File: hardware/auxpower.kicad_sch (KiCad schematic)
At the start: 6 parts

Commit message: review ts
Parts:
- renumbered D22 to D2, D23 to D3, R94 to R13, R95 to R14, TP21 to TP2, TP22 to TP3
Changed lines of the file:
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@@
 		(dnp no)
 		(fields_autoplaced yes)
-		(property "Reference" "R94"
+		(property "Reference" "R13"
 			(at 22.86 118.1099 0)
 			(show_name no)
@@
 			(project "PS-LVCarrier"
 				(path "/9bab2d9d-20f3-40ef-8545-e1299efec47e/194a8848-c0d2-44dd-9e5b-1946509490d6"
-					(reference "R94")
+					(reference "R13")
 					(unit 1)
 				)
@@
 		(dnp no)
 		(fields_autoplaced yes)
-		(property "Reference" "D23"
+		(property "Reference" "D3"
 			(at 39.37 124.3964 90)
 			(show_name no)
@@
 			(project "PS-LVCarrier"
 				(path "/9bab2d9d-20f3-40ef-8545-e1299efec47e/194a8848-c0d2-44dd-9e5b-1946509490d6"
-					(reference "D23")
+					(reference "D3")
 					(unit 1)
 				)
@@
 		(dnp no)
 		(fields_autoplaced yes)
-		(property "Reference" "D22"
+		(property "Reference" "D2"
 			(at 22.86 124.3964 90)
 			(show_name no)
@@
 			(project "PS-LVCarrier"
 				(path "/9bab2d9d-20f3-40ef-8545-e1299efec47e/194a8848-c0d2-44dd-9e5b-1946509490d6"
-					(reference "D22")
+					(reference "D2")
 					(unit 1)
 				)
@@
 		(dnp no)
 		(fields_autoplaced yes)
-		(property "Reference" "#PWR087"
+		(property "Reference" "#PWR018"
 			(at 20.32 119.38 0)
 			(hide yes)
@@
 			(project "PS-LVCarrier"
 				(path "/9bab2d9d-20f3-40ef-8545-e1299efec47e/194a8848-c0d2-44dd-9e5b-1946509490d6"
-					(reference "#PWR087")
+					(reference "#PWR018")
 					(unit 1)
 				)
@@
 		(in_pos_files yes)
 		(dnp no)
-		(property "Reference" "#PWR092"
+		(property "Reference" "#PWR023"
 			(at 157.48 64.77 0)
 			(hide yes)
@@
 			(project "PS-LVCarrier"
 				(path "/9bab2d9d-20f3-40ef-8545-e1299efec47e/194a8848-c0d2-44dd-9e5b-1946509490d6"
-					(reference "#PWR092")
+					(reference "#PWR023")
 					(unit 1)
 				)
@@
 		(dnp no)
 		(fields_autoplaced yes)
-		(property "Reference" "R95"
+		(property "Reference" "R14"
 			(at 39.37 118.1099 0)
 			(show_name no)
@@
 			(project "PS-LVCarrier"
 				(path "/9bab2d9d-20f3-40ef-8545-e1299efec47e/194a8848-c0d2-44dd-9e5b-1946509490d6"
-					(reference "R95")
+					(reference "R14")
 					(unit 1)
 				)
@@
 		(in_pos_files yes)
 		(dnp no)
-		(property "Reference" "#PWR088"
+		(property "Reference" "#PWR019"
 			(at 36.83 119.38 0)
 			(hide yes)
@@
 			(project "PS-LVCarrier"
 				(path "/9bab2d9d-20f3-40ef-8545-e1299efec47e/194a8848-c0d2-44dd-9e5b-1946509490d6"
-					(reference "#PWR088")
+					(reference "#PWR019")
 					(unit 1)
 				)
@@
 		(dnp no)
 		(fields_autoplaced yes)
-		(property "Reference" "#PWR089"
+		(property "Reference" "#PWR020"
 			(at 63.5 123.19 0)
 			(hide yes)
@@
 			(project "PS-LVCarrier"
 				(path "/9bab2d9d-20f3-40ef-8545-e1299efec47e/194a8848-c0d2-44dd-9e5b-1946509490d6"
-					(reference "#PWR089")
+					(reference "#PWR020")
 					(unit 1)
 				)
@@
 		(in_pos_files yes)
 		(dnp no)
-		(property "Reference" "#PWR090"
+		(property "Reference" "#PWR021"
 			(at 74.93 123.19 0)
 			(hide yes)
@@
 			(project "PS-LVCarrier"
 				(path "/9bab2d9d-20f3-40ef-8545-e1299efec47e/194a8848-c0d2-44dd-9e5b-1946509490d6"
-					(reference "#PWR090")
+					(reference "#PWR021")
 					(unit 1)
 				)
@@
 		(dnp no)
 		(fields_autoplaced yes)
-		(property "Reference" "TP22"
+		(property "Reference" "TP3"
 			(at 77.47 121.4119 0)
 			(show_name no)
@@
 			(project "PS-LVCarrier"
 				(path "/9bab2d9d-20f3-40ef-8545-e1299efec47e/194a8848-c0d2-44dd-9e5b-1946509490d6"
-					(reference "TP22")
+					(reference "TP3")
 					(unit 1)
 				)
@@
 		(dnp no)
 		(fields_autoplaced yes)
-		(property "Reference" "#PWR091"
+		(property "Reference" "#PWR022"
 			(at 110.49 64.77 0)
 			(hide yes)
@@
 			(project "PS-LVCarrier"
 				(path "/9bab2d9d-20f3-40ef-8545-e1299efec47e/194a8848-c0d2-44dd-9e5b-1946509490d6"
-					(reference "#PWR091")
+					(reference "#PWR022")
 					(unit 1)
 				)
@@
 		(dnp no)
 		(fields_autoplaced yes)
-		(property "Reference" "TP21"
+		(property "Reference" "TP2"
 			(at 66.04 121.4119 0)
 			(show_name no)
@@
 			(project "PS-LVCarrier"
 				(path "/9bab2d9d-20f3-40ef-8545-e1299efec47e/194a8848-c0d2-44dd-9e5b-1946509490d6"
-					(reference "TP21")
-					(unit 1)
-				)
+					(reference "TP2")
+					(unit 1)
+				)

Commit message: addressed
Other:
- sheet 12V -> 5V Buck Converter ports: added V_in_12V; removed V_in_24V
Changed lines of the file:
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@@
-			)
-		)
-		(pin "V_in_24V" input
-			(at 69.85 60.96 180)
-			(effects
-				(font
-					(size 1.27 1.27)
-				)
-				(justify left)
 			)
 		)
@@
 			)
 		)
+		(pin "V_in_12V" input
+			(at 69.85 60.96 180)
+			(effects
+				(font
+					(size 1.27 1.27)
+				)
+				(justify left)
+			)
+		)

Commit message: try smth on laptop
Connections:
- net +5V renamed 12V -> 5V Buck Converter/V_out_5V
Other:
- note removed: "Indicator LEDs"
- note removed: "Test Points"
- moved on the sheet: D2, D3, R13, R14, TP2, TP3

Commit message: craigenyah
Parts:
- renumbered D2 to D33, D3 to D34, R13 to R116, R14 to R117, TP2 to TP43, TP3 to TP44
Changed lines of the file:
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@@
 		(dnp no)
 		(fields_autoplaced yes)
-		(property "Reference" "R13"
+		(property "Reference" "R116"
 			(at 101.6 66.0399 0)
 			(show_name no)
@@
 			(project "PS-LVCarrier"
 				(path "/9bab2d9d-20f3-40ef-8545-e1299efec47e/194a8848-c0d2-44dd-9e5b-1946509490d6"
-					(reference "R13")
+					(reference "R116")
 					(unit 1)
 				)
@@
 		(dnp no)
 		(fields_autoplaced yes)
-		(property "Reference" "D3"
+		(property "Reference" "D34"
 			(at 156.21 72.3264 90)
 			(show_name no)
@@
 			(project "PS-LVCarrier"
 				(path "/9bab2d9d-20f3-40ef-8545-e1299efec47e/194a8848-c0d2-44dd-9e5b-1946509490d6"
-					(reference "D3")
+					(reference "D34")
 					(unit 1)
 				)
@@
 		(dnp no)
 		(fields_autoplaced yes)
-		(property "Reference" "D2"
+		(property "Reference" "D33"
 			(at 101.6 72.3264 90)
 			(show_name no)
@@
 			(project "PS-LVCarrier"
 				(path "/9bab2d9d-20f3-40ef-8545-e1299efec47e/194a8848-c0d2-44dd-9e5b-1946509490d6"
-					(reference "D2")
+					(reference "D33")
 					(unit 1)
 				)
@@
 		(in_pos_files yes)
 		(dnp no)
-		(property "Reference" "#PWR023"
+		(property "Reference" "#PWR045"
 			(at 147.32 64.77 0)
 			(hide yes)
@@
 			(project "PS-LVCarrier"
 				(path "/9bab2d9d-20f3-40ef-8545-e1299efec47e/194a8848-c0d2-44dd-9e5b-1946509490d6"
-					(reference "#PWR023")
+					(reference "#PWR045")
 					(unit 1)
 				)
@@
 		(dnp no)
 		(fields_autoplaced yes)
-		(property "Reference" "R14"
+		(property "Reference" "R117"
 			(at 156.21 66.0399 0)
 			(show_name no)
@@
 			(project "PS-LVCarrier"
 				(path "/9bab2d9d-20f3-40ef-8545-e1299efec47e/194a8848-c0d2-44dd-9e5b-1946509490d6"
-					(reference "R14")
+					(reference "R117")
 					(unit 1)
 				)
@@
 		(dnp no)
 		(fields_autoplaced yes)
-		(property "Reference" "TP3"
+		(property "Reference" "TP44"
 			(at 156.21 56.3879 0)
 			(show_name no)
@@
 			(project "PS-LVCarrier"
 				(path "/9bab2d9d-20f3-40ef-8545-e1299efec47e/194a8848-c0d2-44dd-9e5b-1946509490d6"
-					(reference "TP3")
+					(reference "TP44")
 					(unit 1)
 				)
@@
 		(dnp no)
 		(fields_autoplaced yes)
-		(property "Reference" "TP2"
+		(property "Reference" "TP43"
 			(at 101.6 56.3879 0)
 			(show_name no)
@@
 			(project "PS-LVCarrier"
 				(path "/9bab2d9d-20f3-40ef-8545-e1299efec47e/194a8848-c0d2-44dd-9e5b-1946509490d6"
-					(reference "TP2")
+					(reference "TP43")
 					(unit 1)
 				)

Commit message: switch, stll working
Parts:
- TP43, TP44: footprint TestPoint:TestPoint_THTPad_D3.0mm_Drill1.5mm -> TestPoint:TestPoint_Loop_D2.50mm_Drill1.0mm_LowProfile
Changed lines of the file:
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@@
 			)
 		)
-		(property "Footprint" "TestPoint:TestPoint_THTPad_D3.0mm_Drill1.5mm"
+		(property "Footprint" "TestPoint:TestPoint_Loop_D2.50mm_Drill1.0mm_LowProfile"
 			(at 158.75 60.96 0)
 			(hide yes)
@@
 			)
 		)
-		(property "Footprint" "TestPoint:TestPoint_THTPad_D3.0mm_Drill1.5mm"
+		(property "Footprint" "TestPoint:TestPoint_Loop_D2.50mm_Drill1.0mm_LowProfile"
 			(at 104.14 60.96 0)
 			(hide yes)

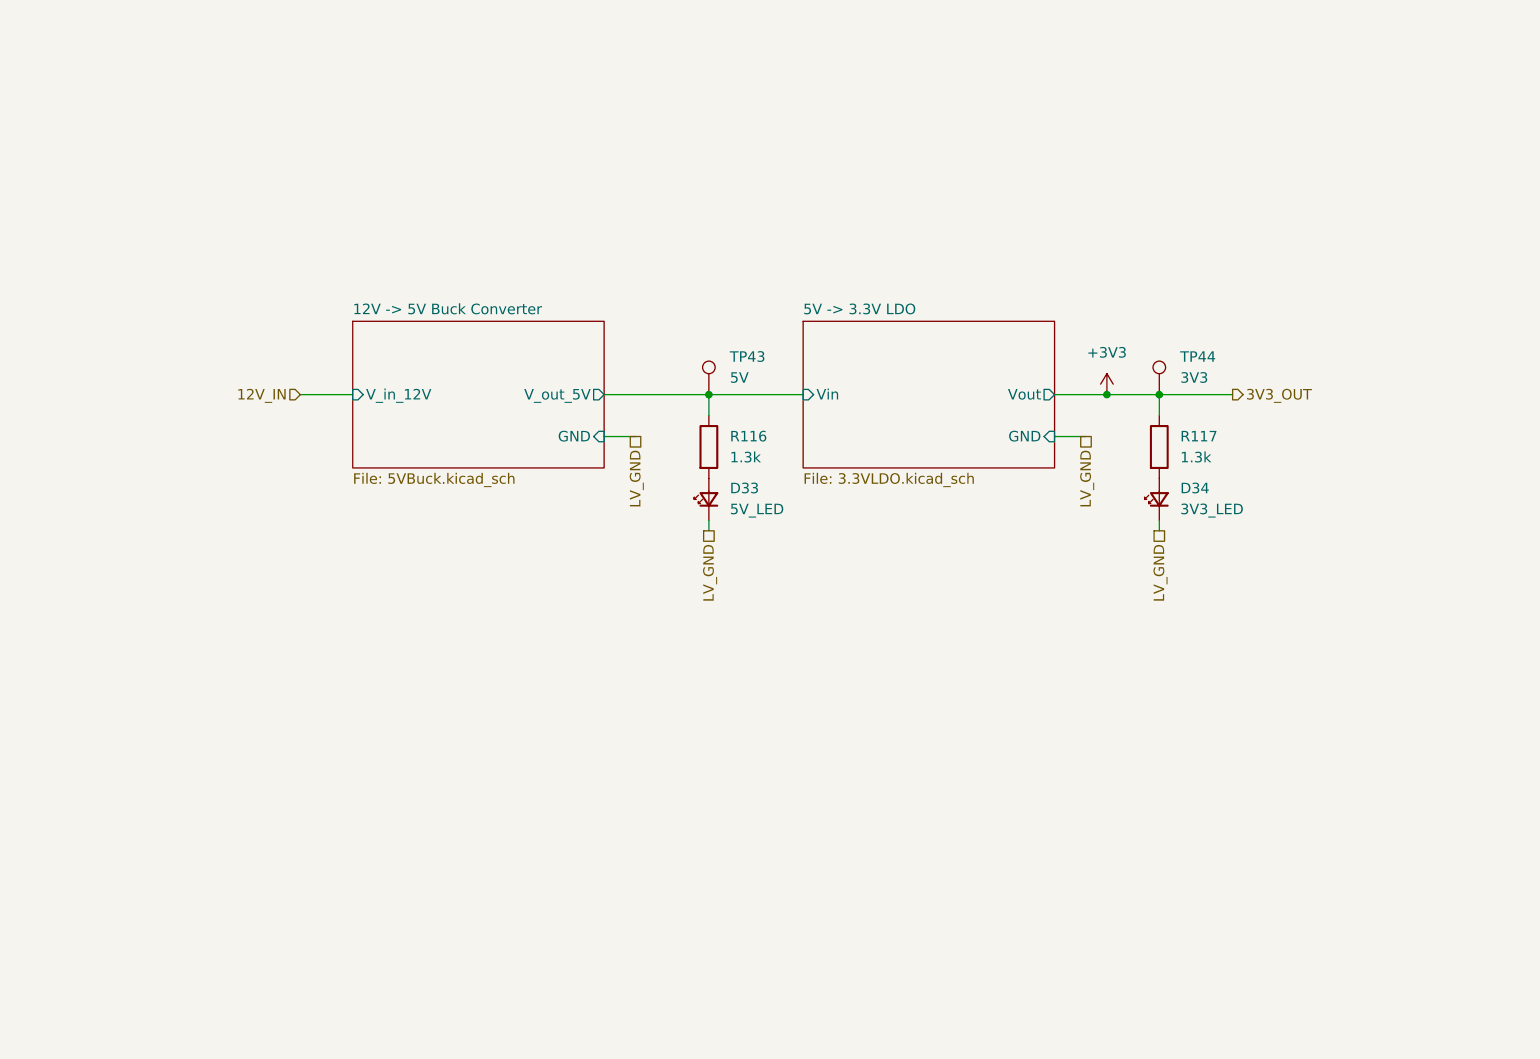
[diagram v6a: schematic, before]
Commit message: switch to laptop
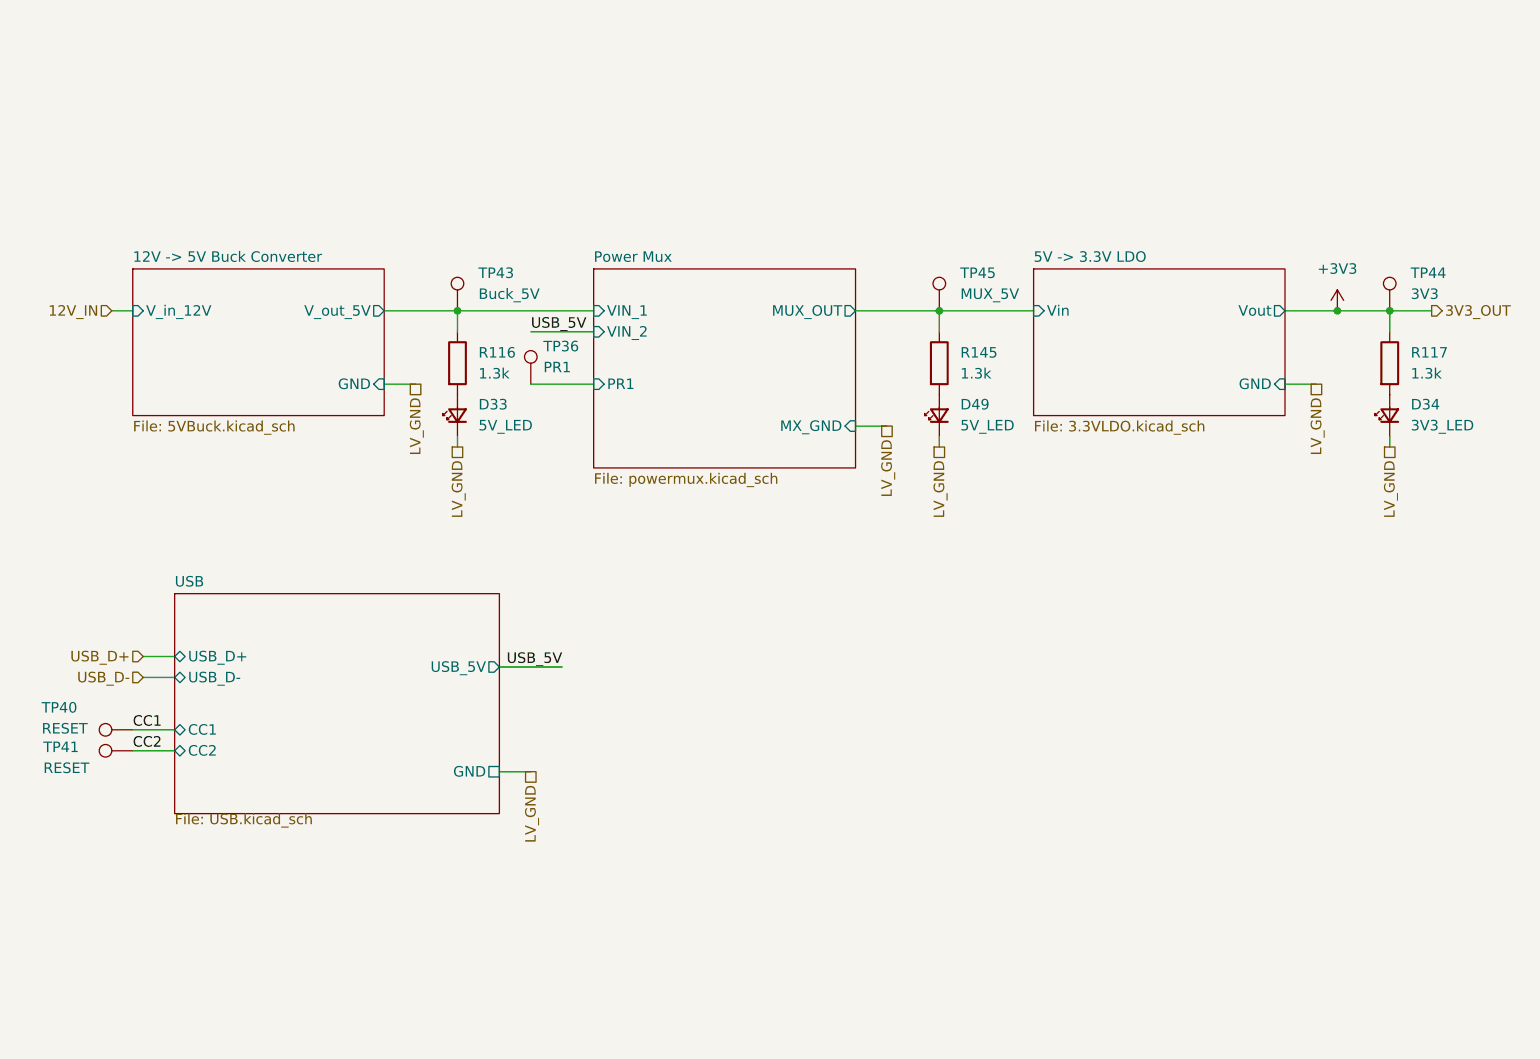
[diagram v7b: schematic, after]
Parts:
- added D49: 5V_LED, LED_SMD:LED_0603_1608Metric_Pad1.05x0.95mm_HandSolder, symbol Device:LED_Small
- added R145: 1.3k, Resistor_SMD:R_0603_1608Metric_Pad0.98x0.95mm_HandSolder, symbol Device:R
- added TP36: PR1, TestPoint:TestPoint_Loop_D2.50mm_Drill1.0mm_LowProfile, symbol Connector:TestPoint
- added TP40, TP41: RESET, TestPoint:TestPoint_Loop_D2.50mm_Drill1.0mm_LowProfile, symbol Connector:TestPoint
- added TP45: MUX_5V, TestPoint:TestPoint_Loop_D2.50mm_Drill1.0mm_LowProfile, symbol Connector:TestPoint
- TP43: value 5V -> Buck_5V
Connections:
- net LV_GND: now also D49.1 (K)
- new net: D49.2 (A), R145.2
- new net 5V -> 3.3V LDO/Vin: R145.1, TP45.1
- new net CC1: TP40.1
- new net CC2: TP41.1
- new net Power Mux/PR1: TP36.1
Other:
- added sheet Power Mux (powermux.kicad_sch)
- added sheet USB (USB.kicad_sch)
- moved on the sheet: D33, D34, R116, R117, TP43, TP44

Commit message: remapped pins
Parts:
- removed TP40, TP41: RESET, TestPoint:TestPoint_Loop_D2.50mm_Drill1.0mm_LowProfile, symbol Connector:TestPoint
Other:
- sheet USB ports: added none; removed CC1, CC2
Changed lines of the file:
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@@
 	(wire
 		(pts
-			(xy 29.21 101.6) (xy 34.29 101.6)
+			(xy 77.47 53.34) (xy 85.09 53.34)
 		)
 		(stroke
@@
 	(wire
 		(pts
-			(xy 77.47 53.34) (xy 85.09 53.34)
+			(xy 181.61 66.04) (xy 181.61 67.31)
 		)
 		(stroke
@@
 	(wire
 		(pts
-			(xy 181.61 66.04) (xy 181.61 67.31)
-		)
-		(stroke
-			(width 0)
-			(type default)
-		)
-	)
-	(wire
-		(pts
 			(xy 116.84 50.8) (xy 127 50.8)
-		)
-		(stroke
-			(width 0)
-			(type default)
-		)
-	)
-	(wire
-		(pts
-			(xy 29.21 104.14) (xy 34.29 104.14)
 		)
 		(stroke
@@
 	(label "USB_5V"
 		(at 77.47 53.34 0)
-		(effects
-			(font
-				(size 1.27 1.27)
-			)
-			(justify left bottom)
-		)
-	)
-	(label "CC1"
-		(at 29.21 101.6 0)
-		(effects
-			(font
-				(size 1.27 1.27)
-			)
-			(justify left bottom)
-		)
-	)
-	(label "CC2"
-		(at 29.21 104.14 0)
 		(effects
 			(font
@@
 	)
 	(symbol
-		(lib_id "Connector:TestPoint")
-		(at 29.21 101.6 90)
-		(unit 1)
-		(body_style 1)
-		(exclude_from_sim no)
-		(in_bom yes)
-		(on_board yes)
-		(in_pos_files yes)
-		(dnp no)
-		(property "Reference" "TP40"
-			(at 18.1609 98.9199 90)
-			(show_name no)
-			(do_not_autoplace no)
-			(effects
-				(font
-					(size 1.27 1.27)
-				)
-				(justify right)
-			)
-		)
-		(property "Value" "RESET"
-			(at 18.1609 101.4599 90)
-			(show_name no)
-			(do_not_autoplace no)
-			(effects
-				(font
-					(size 1.27 1.27)
-				)
-				(justify right)
-			)
-		)
-		(property "Footprint" "TestPoint:TestPoint_Loop_D2.50mm_Drill1.0mm_LowProfile"
-			(at 29.21 96.52 0)
-			(hide yes)
-			(show_name no)
-			(do_not_autoplace no)
-			(effects
-				(font
-					(size 1.27 1.27)
-				)
-			)
-		)
-		(property "Datasheet" ""
-			(at 29.21 96.52 0)
-			(hide yes)
-			(show_name no)
-			(do_not_autoplace no)
-			(effects
-				(font
-					(size 1.27 1.27)
-				)
-			)
-		)
-		(property "Description" "test point"
-			(at 29.21 101.6 0)
-			(hide yes)
-			(show_name no)
-			(do_not_autoplace no)
-			(effects
-				(font
-					(size 1.27 1.27)
-				)
-			)
-		)
-		(property "LCSC" ""
-			(at 29.21 101.6 0)
-			(hide yes)
-			(show_name no)
-			(do_not_autoplace no)
-			(effects
-				(font
-					(size 1.27 1.27)
-				)
-			)
-		)
-		(pin "1"
-		)
-		(instances
-			(project "PS-LVCarrier"
-				(path "/9bab2d9d-20f3-40ef-8545-e1299efec47e/194a8848-c0d2-44dd-9e5b-1946509490d6"
-					(reference "TP40")
-					(unit 1)
-				)
-			)
-		)
-	)
-	(symbol
 		(lib_id "Device:LED_Small")
 		(at 127 63.5 90)
@@
 				(path "/9bab2d9d-20f3-40ef-8545-e1299efec47e/194a8848-c0d2-44dd-9e5b-1946509490d6"
 					(reference "D49")
-					(unit 1)
-				)
-			)
-		)
-	)
-	(symbol
-		(lib_id "Connector:TestPoint")
-		(at 29.21 104.14 90)
-		(unit 1)
-		(body_style 1)
-		(exclude_from_sim no)
-		(in_bom yes)
-		(on_board yes)
-		(in_pos_files yes)
-		(dnp no)
-		(property "Reference" "TP41"
-			(at 18.3618 103.7083 90)
-			(show_name no)
-			(do_not_autoplace no)
-			(effects
-				(font
-					(size 1.27 1.27)
-				)
-				(justify right)
-			)
-		)
-		(property "Value" "RESET"
-			(at 18.3618 106.2483 90)
-			(show_name no)
-			(do_not_autoplace no)
-			(effects
-				(font
-					(size 1.27 1.27)
-				)
-				(justify right)
-			)
-		)
-		(property "Footprint" "TestPoint:TestPoint_Loop_D2.50mm_Drill1.0mm_LowProfile"
-			(at 29.21 99.06 0)
-			(hide yes)
-			(show_name no)
-			(do_not_autoplace no)
-			(effects
-				(font
-					(size 1.27 1.27)
-				)
-			)
-		)
-		(property "Datasheet" ""
-			(at 29.21 99.06 0)
-			(hide yes)
-			(show_name no)
-			(do_not_autoplace no)
-			(effects
-				(font
-					(size 1.27 1.27)
-				)
-			)
-		)
-		(property "Description" "test point"
-			(at 29.21 104.14 0)
-			(hide yes)
-			(show_name no)
-			(do_not_autoplace no)
-			(effects
-				(font
-					(size 1.27 1.27)
-				)
-			)
-		)
-		(property "LCSC" ""
-			(at 29.21 104.14 0)
-			(hide yes)
-			(show_name no)
-			(do_not_autoplace no)
-			(effects
-				(font
-					(size 1.27 1.27)
-				)
-			)
-		)
-		(pin "1"
-		)
-		(instances
-			(project "PS-LVCarrier"
-				(path "/9bab2d9d-20f3-40ef-8545-e1299efec47e/194a8848-c0d2-44dd-9e5b-1946509490d6"
-					(reference "TP41")
 					(unit 1)
 				)
@@
 			)
 		)
-		(pin "CC1" bidirectional
-			(at 34.29 101.6 180)
-			(effects
-				(font
-					(size 1.27 1.27)
-				)
-				(justify left)
-			)
-		)
-		(pin "CC2" bidirectional
-			(at 34.29 104.14 180)
-			(effects
-				(font
-					(size 1.27 1.27)
-				)
-				(justify left)
-			)
-		)
